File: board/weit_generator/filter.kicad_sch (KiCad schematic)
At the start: 5 parts, among them U1 MCP6004

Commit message: New layout
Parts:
- removed U1: MCP6004, Package_DIP:DIP-14_W7.62mm_Socket_LongPads, symbol Amplifier_Operational:MCP6004
- added R22: 100, Resistor_THT:R_Axial_DIN0207_L6.3mm_D2.5mm_P2.54mm_Vertical, symbol Device:R
- added U?: MCP6004, Package_DIP:DIP-14_W7.62mm_Socket, symbol Amplifier_Operational:MCP6004
- C?: footprint Capacitor_THT:C_Rect_L9.0mm_W4.0mm_P7.50mm_MKT -> Capacitor_THT:C_Rect_L13.0mm_W4.0mm_P10.00mm_FKS3_FKP3_MKS4; Dielectric (none) -> Polysterene
- C?: footprint Capacitor_THT:C_Rect_L9.0mm_W4.0mm_P7.50mm_MKT -> Capacitor_THT:C_Rect_L13.0mm_W4.0mm_P10.00mm_FKS3_FKP3_MKS4; Dielectric (none) -> Polistyrene
- R? (x2): footprint Resistor_SMD:R_0805_2012Metric_Pad1.20x1.40mm_HandSolder -> Resistor_THT:R_Axial_DIN0207_L6.3mm_D2.5mm_P2.54mm_Vertical
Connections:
- net OUT: now also R22.2
- net at C?.1, C?.2, R?.2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: now also U?.3 (+)
- new net: R22.1, U?.1, U?.2 (-)
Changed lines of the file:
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@@
   (junction (at 125.095 96.52) (diameter 0) (color 0 0 0 0)
   )
-  (wire (pts (xy 169.545 99.06) (xy 165.1 99.06))
+  (wire (pts (xy 189.23 99.06) (xy 184.15 99.06))
     (stroke (width 0) (type default))
   )
@@
   )
   (wire (pts (xy 165.1 106.68) (xy 145.415 106.68))
+    (stroke (width 0) (type default))
+  )
+  (wire (pts (xy 176.53 99.06) (xy 165.1 99.06))
     (stroke (width 0) (type default))
   )
@@
     (effects (font (size 1.27 1.27)) (justify right))
   )
-  (hierarchical_label "OUT" (shape input) (at 169.545 99.06 0) (fields_autoplaced)
+  (hierarchical_label "OUT" (shape input) (at 189.23 99.06 0) (fields_autoplaced)
     (effects (font (size 1.27 1.27)) (justify left))
   )
@@
       (effects (font (size 1.27 1.27)))
     )
-    (property "Footprint" "Capacitor_THT:C_Rect_L9.0mm_W4.0mm_P7.50mm_MKT" (at 113.03 97.4852 0)
+    (property "Footprint" "Capacitor_THT:C_Rect_L13.0mm_W4.0mm_P10.00mm_FKS3_FKP3_MKS4" (at 113.03 97.4852 0)
       (effects (font (size 1.27 1.27)) hide)
     )
@@
       (effects (font (size 1.27 1.27)) hide)
     )
+    (property "Dielectric" "Polysterene" (at 116.84 96.52 90)
+      (effects (font (size 1.27 1.27)) hide)
+    )
     (pin "1")
     (pin "2")
@@
         )
         (path "/b85c55a9-e1f6-4dbf-a795-73634abf8d52/bc867f68-0e73-45d0-a69e-b51a7f01f5c2"
-          (reference "C5") (unit 1)
+          (reference "C8") (unit 1)
         )
       )
@@
       (effects (font (size 1.27 1.27)) (justify left))
     )
-    (property "Footprint" "Resistor_SMD:R_0805_2012Metric_Pad1.20x1.40mm_HandSolder" (at 123.317 91.44 90)
+    (property "Footprint" "Resistor_THT:R_Axial_DIN0207_L6.3mm_D2.5mm_P2.54mm_Vertical" (at 123.317 91.44 90)
       (effects (font (size 1.27 1.27)) hide)
     )
@@
         )
         (path "/b85c55a9-e1f6-4dbf-a795-73634abf8d52/bc867f68-0e73-45d0-a69e-b51a7f01f5c2"
-          (reference "R19") (unit 1)
+          (reference "R20") (unit 1)
+        )
+      )
+    )
+  )
+  (symbol (lib_id "Device:R") (at 180.34 99.06 90) (unit 1)
+    (in_bom yes) (on_board yes) (dnp no) (fields_autoplaced)
+    (property "Reference" "R22" (at 180.34 93.98 90)
+      (effects (font (size 1.27 1.27)))
+    )
+    (property "Value" "100" (at 180.34 96.52 90)
+      (effects (font (size 1.27 1.27)))
+    )
+    (property "Footprint" "Resistor_THT:R_Axial_DIN0207_L6.3mm_D2.5mm_P2.54mm_Vertical" (at 180.34 100.838 90)
+      (effects (font (size 1.27 1.27)) hide)
+    )
+    (property "Datasheet" "~" (at 180.34 99.06 0)
+      (effects (font (size 1.27 1.27)) hide)
+    )
+    (pin "1")
+    (pin "2")
+    (instances
+      (project "weit_generator"
+        (path "/b85c55a9-e1f6-4dbf-a795-73634abf8d52/bc867f68-0e73-45d0-a69e-b51a7f01f5c2"
+          (reference "R22") (unit 1)
         )
       )
@@
       (effects (font (size 1.27 1.27)) (justify right))
     )
-    (property "Footprint" "Resistor_SMD:R_0805_2012Metric_Pad1.20x1.40mm_HandSolder" (at 126.873 102.235 90)
+    (property "Footprint" "Resistor_THT:R_Axial_DIN0207_L6.3mm_D2.5mm_P2.54mm_Vertical" (at 126.873 102.235 90)
       (effects (font (size 1.27 1.27)) hide)
     )
@@
         )
         (path "/b85c55a9-e1f6-4dbf-a795-73634abf8d52/bc867f68-0e73-45d0-a69e-b51a7f01f5c2"
-          (reference "R20") (unit 1)
-        )
-      )
-    )
-  )
-  (symbol (lib_id "Device:C") (at 135.89 100.33 180) (unit 1)
-    (in_bom yes) (on_board yes) (dnp no) (fields_autoplaced)
-    (property "Reference" "C?" (at 139.065 99.695 0)
-      (effects (font (size 1.27 1.27)) (justify right))
-    )
-    (property "Value" "10n" (at 139.065 102.235 0)
-      (effects (font (size 1.27 1.27)) (justify right))
-    )
-    (property "Footprint" "Capacitor_THT:C_Rect_L9.0mm_W4.0mm_P7.50mm_MKT" (at 134.9248 96.52 0)
-      (effects (font (size 1.27 1.27)) hide)
-    )
-    (property "Datasheet" "~" (at 135.89 100.33 0)
-      (effects (font (size 1.27 1.27)) hide)
-    )
-    (pin "1")
-    (pin "2")
-    (instances
-      (project "weit_generator"
-        (path "/b85c55a9-e1f6-4dbf-a795-73634abf8d52"
-          (reference "C?") (unit 1)
-        )
-        (path "/b85c55a9-e1f6-4dbf-a795-73634abf8d52/bc867f68-0e73-45d0-a69e-b51a7f01f5c2"
-          (reference "C4") (unit 1)
-        )
-      )
-    )
-  )
-  (symbol (lib_id "power:GND") (at 125.095 106.045 0) (unit 1)
-    (in_bom yes) (on_board yes) (dnp no) (fields_autoplaced)
-    (property "Reference" "#PWR?" (at 125.095 112.395 0)
-      (effects (font (size 1.27 1.27)) hide)
-    )
-    (property "Value" "GND" (at 125.095 111.125 0)
-      (effects (font (size 1.27 1.27)))
-    )
-    (property "Footprint" "" (at 125.095 106.045 0)
-      (effects (font (size 1.27 1.27)) hide)
-    )
-    (property "Datasheet" "" (at 125.095 106.045 0)
-      (effects (font (size 1.27 1.27)) hide)
-    )
-    (pin "1")
-    (instances
-      (project "weit_generator"
-        (path "/b85c55a9-e1f6-4dbf-a795-73634abf8d52"
-          (reference "#PWR?") (unit 1)
-        )
-        (path "/b85c55a9-e1f6-4dbf-a795-73634abf8d52/bc867f68-0e73-45d0-a69e-b51a7f01f5c2"
-          (reference "#PWR023") (unit 1)
-        )
-      )
-    )
-  )
-  (symbol (lib_id "Amplifier_Operational:MCP6004") (at 154.305 99.06 0) (unit 2)
-    (in_bom yes) (on_board yes) (dnp no) (fields_autoplaced)
-    (property "Reference" "U1" (at 154.305 89.535 0)
+          (reference "R21") (unit 1)
+        )
+      )
+    )
+  )
+  (symbol (lib_id "Amplifier_Operational:MCP6004") (at 154.305 99.06 0) (unit 1)
+    (in_bom yes) (on_board yes) (dnp no) (fields_autoplaced)
+    (property "Reference" "U?" (at 154.305 89.535 0)
       (effects (font (size 1.27 1.27)))
     )
@@
       (effects (font (size 1.27 1.27)))
     )
-    (property "Footprint" "Package_DIP:DIP-14_W7.62mm_Socket_LongPads" (at 153.035 96.52 0)
+    (property "Footprint" "Package_DIP:DIP-14_W7.62mm_Socket" (at 153.035 96.52 0)
       (effects (font (size 1.27 1.27)) hide)
     )
@@
       (project "weit_generator"
         (path "/b85c55a9-e1f6-4dbf-a795-73634abf8d52"
-          (reference "U1") (unit 2)
-        )
-        (path "/b85c55a9-e1f6-4dbf-a795-73634abf8d52/bc867f68-0e73-45d0-a69e-b51a7f01f5c2"
-          (reference "U1") (unit 2)
+          (reference "U?") (unit 1)
+        )
+        (path "/b85c55a9-e1f6-4dbf-a795-73634abf8d52/bc867f68-0e73-45d0-a69e-b51a7f01f5c2"
+          (reference "U1") (unit 1)
+        )
+      )
+    )
+  )
+  (symbol (lib_id "Device:C") (at 135.89 100.33 180) (unit 1)
+    (in_bom yes) (on_board yes) (dnp no) (fields_autoplaced)
+    (property "Reference" "C?" (at 139.065 99.695 0)
+      (effects (font (size 1.27 1.27)) (justify right))
+    )
+    (property "Value" "10n" (at 139.065 102.235 0)
+      (effects (font (size 1.27 1.27)) (justify right))
+    )
+    (property "Footprint" "Capacitor_THT:C_Rect_L13.0mm_W4.0mm_P10.00mm_FKS3_FKP3_MKS4" (at 134.9248 96.52 0)
+      (effects (font (size 1.27 1.27)) hide)
+    )
+    (property "Datasheet" "~" (at 135.89 100.33 0)
+      (effects (font (size 1.27 1.27)) hide)
+    )
+    (property "Dielectric" "Polistyrene" (at 135.89 100.33 0)
+      (effects (font (size 1.27 1.27)) hide)
+    )
+    (pin "1")
+    (pin "2")
+    (instances
+      (project "weit_generator"
+        (path "/b85c55a9-e1f6-4dbf-a795-73634abf8d52"
+          (reference "C?") (unit 1)
+        )
+        (path "/b85c55a9-e1f6-4dbf-a795-73634abf8d52/bc867f68-0e73-45d0-a69e-b51a7f01f5c2"
+          (reference "C9") (unit 1)
+        )
+      )
+    )
+  )
+  (symbol (lib_id "power:GND") (at 125.095 106.045 0) (unit 1)
+    (in_bom yes) (on_board yes) (dnp no) (fields_autoplaced)
+    (property "Reference" "#PWR?" (at 125.095 112.395 0)
+      (effects (font (size 1.27 1.27)) hide)
+    )
+    (property "Value" "GND" (at 125.095 111.125 0)
+      (effects (font (size 1.27 1.27)))
+    )
+    (property "Footprint" "" (at 125.095 106.045 0)
+      (effects (font (size 1.27 1.27)) hide)
+    )
+    (property "Datasheet" "" (at 125.095 106.045 0)
+      (effects (font (size 1.27 1.27)) hide)
+    )
+    (pin "1")
+    (instances
+      (project "weit_generator"
+        (path "/b85c55a9-e1f6-4dbf-a795-73634abf8d52"
+          (reference "#PWR?") (unit 1)
+        )
+        (path "/b85c55a9-e1f6-4dbf-a795-73634abf8d52/bc867f68-0e73-45d0-a69e-b51a7f01f5c2"
+          (reference "#PWR033") (unit 1)
         )
       )
@@
         )
         (path "/b85c55a9-e1f6-4dbf-a795-73634abf8d52/bc867f68-0e73-45d0-a69e-b51a7f01f5c2"
-          (reference "#PWR022") (unit 1)
+          (reference "#PWR032") (unit 1)
         )
       )
@@
         )
         (path "/b85c55a9-e1f6-4dbf-a795-73634abf8d52/bc867f68-0e73-45d0-a69e-b51a7f01f5c2"
-          (reference "#PWR016") (unit 1)
-        )
-      )
+          (reference "#PWR034") (unit 1)
+        )
+      )

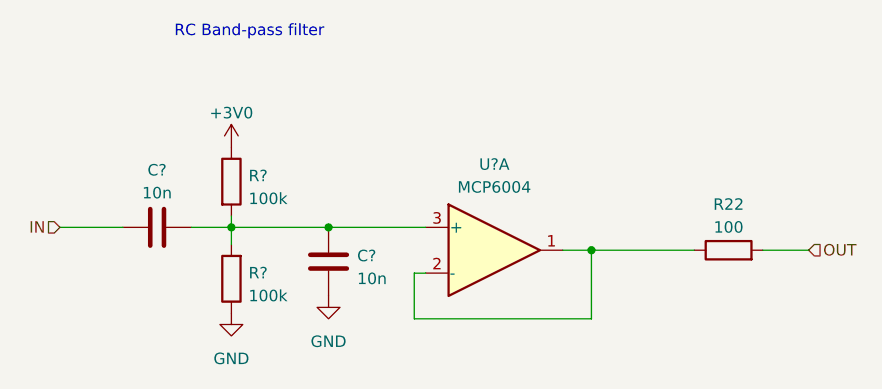
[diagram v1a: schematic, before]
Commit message: finished board, added test desription and tuning to docs
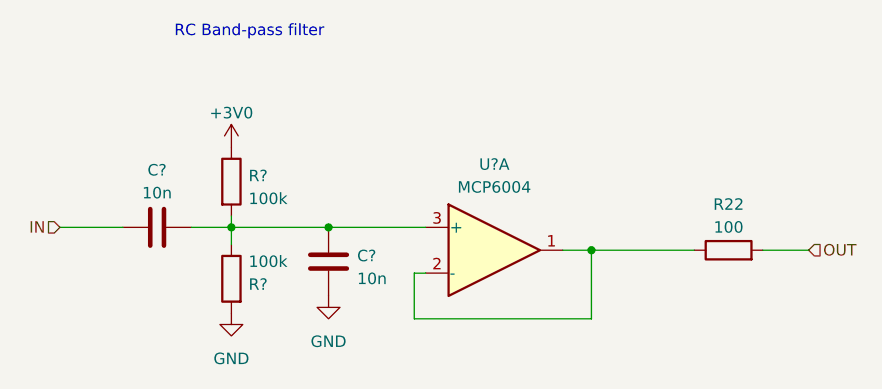
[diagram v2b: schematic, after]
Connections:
- net GND: now also R?.2; no longer R?.1
- net at C?.1, C?.2, R?.2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: now also R?.1; no longer R?.2
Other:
- moved on the sheet: R?
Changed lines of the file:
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@@
     )
   )
-  (symbol (lib_id "Device:R") (at 125.095 102.235 180) (unit 1)
-    (in_bom yes) (on_board yes) (dnp no) (fields_autoplaced)
-    (property "Reference" "R?" (at 127 101.6 0)
+  (symbol (lib_id "Device:R") (at 125.095 102.235 0) (mirror y) (unit 1)
+    (in_bom yes) (on_board yes) (dnp no)
+    (property "Reference" "R?" (at 127 102.87 0)
       (effects (font (size 1.27 1.27)) (justify right))
     )
-    (property "Value" "100k" (at 127 104.14 0)
+    (property "Value" "100k" (at 127 100.33 0)
       (effects (font (size 1.27 1.27)) (justify right))
     )

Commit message: .
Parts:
- renumbered R22 to R21
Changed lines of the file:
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@@
         )
         (path "/b85c55a9-e1f6-4dbf-a795-73634abf8d52/bc867f68-0e73-45d0-a69e-b51a7f01f5c2"
-          (reference "C8") (unit 1)
+          (reference "C7") (unit 1)
         )
       )
@@
         )
         (path "/b85c55a9-e1f6-4dbf-a795-73634abf8d52/bc867f68-0e73-45d0-a69e-b51a7f01f5c2"
-          (reference "R20") (unit 1)
+          (reference "R19") (unit 1)
         )
       )
@@
   (symbol (lib_id "Device:R") (at 180.34 99.06 90) (unit 1)
     (in_bom yes) (on_board yes) (dnp no) (fields_autoplaced)
-    (property "Reference" "R22" (at 180.34 93.98 90)
+    (property "Reference" "R21" (at 180.34 93.98 90)
       (effects (font (size 1.27 1.27)))
     )
@@
       (project "weit_generator"
         (path "/b85c55a9-e1f6-4dbf-a795-73634abf8d52/bc867f68-0e73-45d0-a69e-b51a7f01f5c2"
-          (reference "R22") (unit 1)
+          (reference "R21") (unit 1)
         )
       )
@@
         )
         (path "/b85c55a9-e1f6-4dbf-a795-73634abf8d52/bc867f68-0e73-45d0-a69e-b51a7f01f5c2"
-          (reference "R21") (unit 1)
+          (reference "R17") (unit 1)
         )
       )
@@
         )
         (path "/b85c55a9-e1f6-4dbf-a795-73634abf8d52/bc867f68-0e73-45d0-a69e-b51a7f01f5c2"
-          (reference "U1") (unit 1)
+          (reference "U2") (unit 1)
         )
       )
@@
         )
         (path "/b85c55a9-e1f6-4dbf-a795-73634abf8d52/bc867f68-0e73-45d0-a69e-b51a7f01f5c2"
-          (reference "C9") (unit 1)
+          (reference "C8") (unit 1)
         )
       )

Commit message: .
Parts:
- removed C?: 10n, Capacitor_THT:C_Rect_L13.0mm_W4.0mm_P10.00mm_FKS3_FKP3_MKS4, symbol Device:C
- added C1: 100n, Capacitor_THT:C_Rect_L13.0mm_W6.0mm_P10.00mm_FKS3_FKP3_MKS4, symbol Device:C
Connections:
- net IN: now also C1.1
- net at C?.2, R?.1, R?.2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: now also C1.2
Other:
- moved on the sheet: R21
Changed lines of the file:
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@@
   (junction (at 125.095 96.52) (diameter 0) (color 0 0 0 0)
   )
-  (wire (pts (xy 189.23 99.06) (xy 184.15 99.06))
+  (wire (pts (xy 184.15 99.06) (xy 179.07 99.06))
     (stroke (width 0) (type default))
   )
@@
     (stroke (width 0) (type default))
   )
-  (wire (pts (xy 176.53 99.06) (xy 165.1 99.06))
+  (wire (pts (xy 171.45 99.06) (xy 165.1 99.06))
     (stroke (width 0) (type default))
   )
@@
     (effects (font (size 1.27 1.27)) (justify right))
   )
-  (hierarchical_label "OUT" (shape input) (at 189.23 99.06 0) (fields_autoplaced)
+  (hierarchical_label "OUT" (shape input) (at 184.15 99.06 0) (fields_autoplaced)
     (effects (font (size 1.27 1.27)) (justify left))
-  )
-  (symbol (lib_id "Device:C") (at 116.84 96.52 270) (unit 1)
-    (in_bom yes) (on_board yes) (dnp no) (fields_autoplaced)
-    (property "Reference" "C?" (at 116.84 90.17 90)
-      (effects (font (size 1.27 1.27)))
-    )
-    (property "Value" "10n" (at 116.84 92.71 90)
-      (effects (font (size 1.27 1.27)))
-    )
-    (property "Footprint" "Capacitor_THT:C_Rect_L13.0mm_W4.0mm_P10.00mm_FKS3_FKP3_MKS4" (at 113.03 97.4852 0)
-      (effects (font (size 1.27 1.27)) hide)
-    )
-    (property "Datasheet" "~" (at 116.84 96.52 0)
-      (effects (font (size 1.27 1.27)) hide)
-    )
-    (property "Dielectric" "Polysterene" (at 116.84 96.52 90)
-      (effects (font (size 1.27 1.27)) hide)
-    )
-    (pin "1")
-    (pin "2")
-    (instances
-      (project "weit_generator"
-        (path "/b85c55a9-e1f6-4dbf-a795-73634abf8d52"
-          (reference "C?") (unit 1)
-        )
-        (path "/b85c55a9-e1f6-4dbf-a795-73634abf8d52/bc867f68-0e73-45d0-a69e-b51a7f01f5c2"
-          (reference "C7") (unit 1)
-        )
-      )
-    )
   )
   (symbol (lib_id "Device:R") (at 125.095 91.44 0) (unit 1)
@@
     )
   )
-  (symbol (lib_id "Device:R") (at 180.34 99.06 90) (unit 1)
-    (in_bom yes) (on_board yes) (dnp no) (fields_autoplaced)
-    (property "Reference" "R21" (at 180.34 93.98 90)
-      (effects (font (size 1.27 1.27)))
-    )
-    (property "Value" "100" (at 180.34 96.52 90)
-      (effects (font (size 1.27 1.27)))
-    )
-    (property "Footprint" "Resistor_THT:R_Axial_DIN0207_L6.3mm_D2.5mm_P2.54mm_Vertical" (at 180.34 100.838 90)
-      (effects (font (size 1.27 1.27)) hide)
-    )
-    (property "Datasheet" "~" (at 180.34 99.06 0)
+  (symbol (lib_id "Device:R") (at 175.26 99.06 90) (unit 1)
+    (in_bom yes) (on_board yes) (dnp no) (fields_autoplaced)
+    (property "Reference" "R21" (at 175.26 93.98 90)
+      (effects (font (size 1.27 1.27)))
+    )
+    (property "Value" "100" (at 175.26 96.52 90)
+      (effects (font (size 1.27 1.27)))
+    )
+    (property "Footprint" "Resistor_THT:R_Axial_DIN0207_L6.3mm_D2.5mm_P2.54mm_Vertical" (at 175.26 100.838 90)
+      (effects (font (size 1.27 1.27)) hide)
+    )
+    (property "Datasheet" "~" (at 175.26 99.06 0)
       (effects (font (size 1.27 1.27)) hide)
     )
@@
         )
       )
+    )
+  )
+  (symbol (lib_id "Device:C") (at 116.84 96.52 90) (unit 1)
+    (in_bom yes) (on_board yes) (dnp no) (fields_autoplaced)
+    (property "Reference" "C1" (at 116.84 90.805 90)
+      (effects (font (size 1.27 1.27)))
+    )
+    (property "Value" "100n" (at 116.84 93.345 90)
+      (effects (font (size 1.27 1.27)))
+    )
+    (property "Footprint" "Capacitor_THT:C_Rect_L13.0mm_W6.0mm_P10.00mm_FKS3_FKP3_MKS4" (at 120.65 95.5548 0)
+      (effects (font (size 1.27 1.27)) hide)
+    )
+    (property "Datasheet" "~" (at 116.84 96.52 0)
+      (effects (font (size 1.27 1.27)) hide)
+    )
+    (property "Dielectric" "Polisteryne" (at 116.84 96.52 90)
+      (effects (font (size 1.27 1.27)) hide)
+    )
+    (pin "1")
+    (pin "2")
+    (instances
+      (project "weit_generator"
+        (path "/b85c55a9-e1f6-4dbf-a795-73634abf8d52"
+          (reference "C1") (unit 1)
+        )
+        (path "/b85c55a9-e1f6-4dbf-a795-73634abf8d52/bc867f68-0e73-45d0-a69e-b51a7f01f5c2"
+          (reference "C7") (unit 1)
+        )
+      )

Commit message: WIELKA POLONIAAAAA
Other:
- title: (none) -> Filtr
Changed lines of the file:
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@@
 (kicad_sch (version 20230121) (generator eeschema)
   (paper "A4")
+  (title_block
+    (title "Filtr")
+    (date "2023-04-15")
+    (rev "1.0")
+    (comment 1 "Kondensatory PP/PS")
+  )
   (junction (at 135.89 96.52) (diameter 0) (color 0 0 0 0)
   )

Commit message: Final revision - submitting
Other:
- note added: "Filtr krawędziowy RC"
- note removed: "RC Band-pass filter"
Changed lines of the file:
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@@
     (stroke (width 0) (type default))
   )
-  (text "RC Band-pass filter" (at 118.745 75.565 0)
+  (text "Filtr krawędziowy RC" (at 132.715 79.375 0)
     (effects (font (size 1.27 1.27)) (justify left bottom))
   )
